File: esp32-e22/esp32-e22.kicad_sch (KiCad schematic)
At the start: 20 parts, among them J1 Conn_01x04_Socket, J2 Conn_01x04_Socket, J3 Conn_01x04_Socket, J4 Conn_01x03_Socket, J5 SMA, J6 Conn_01x02_Pin, J7 USB_C_Receptacle_PowerOnly_6P, J8 Conn_01x04_Socket, J9 Conn_01x02_Pin, SW1 SW_Push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

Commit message: fixed some missing footprints -> V2.0.5
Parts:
- removed J6: Conn_01x02_Pin, Connector_PinHeader_2.54mm:PinHeader_1x02_P2.54mm_Vertical, symbol Connector:Conn_01x02_Pin
- removed J9: Conn_01x02_Pin, symbol Connector:Conn_01x02_Pin
- added J6, J9: Conn_01x02_Socket, Connector_PinHeader_2.54mm:PinHeader_1x02_P2.54mm_Vertical, symbol Connector:Conn_01x02_Socket
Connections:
- net +5V: now also J9.1 (Pin_1)
- net GND: now also J6.2 (Pin_2), J9.2 (Pin_2)
- net at U1.8 (DIO2): now also J6.1 (Pin_1)
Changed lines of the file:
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@@
 		(title "ESP32 - E22 Board")
 		(date "2024-10-04")
-		(rev "V2.0.4")
+		(rev "V2.0.5")
 		(company "DK9BT / OE3WAS")
 	)
@@
 	(wire
 		(pts
-			(xy 82.55 149.86) (xy 82.55 153.67)
-		)
-		(stroke
-			(width 0)
-			(type default)
-		)
-	)
-	(wire
-		(pts
 			(xy 53.34 105.41) (xy 194.31 105.41)
 		)
@@
 	(wire
 		(pts
+			(xy 82.55 149.86) (xy 82.55 153.67)
+		)
+		(stroke
+			(width 0)
+			(type default)
+		)
+	)
+	(wire
+		(pts
 			(xy 181.61 58.42) (xy 217.17 58.42)
 		)
@@
 	)
 	(symbol
-		(lib_id "Connector:Conn_01x02_Pin")
-		(at 77.47 147.32 0)
+		(lib_id "power:+3.3V")
+		(at 160.02 85.09 0)
 		(unit 1)
 		(exclude_from_sim no)
@@
 		(on_board yes)
 		(dnp no)
-		(fields_autoplaced yes)
-		(property "Reference" "J9"
-			(at 76.2 148.5899 0)
+		(property "Reference" "#PWR015"
+			(at 160.02 88.9 0)
 			(effects
 				(font
 					(size 1.27 1.27)
 				)
-				(justify right)
+				(hide yes)
 			)
 		)
-		(property "Value" "Conn_01x02_Pin"
-			(at 78.105 144.78 0)
+		(property "Value" "+3.3V"
+			(at 157.734 81.28 0)
 			(effects
 				(font
 					(size 1.27 1.27)
 				)
-				(hide yes)
+				(justify left)
 			)
 		)
 		(property "Footprint" ""
-			(at 77.47 147.32 0)
+			(at 160.02 85.09 0)
 			(effects
 				(font
@@
 			)
 		)
-		(property "Datasheet" "~"
-			(at 77.47 147.32 0)
+		(property "Datasheet" ""
+			(at 160.02 85.09 0)
 			(effects
 				(font
@@
 			)
 		)
-		(property "Description" "Generic connector, single row, 01x02, script generated"
-			(at 77.47 147.32 0)
+		(property "Description" "Power symbol creates a global label with name \"+3.3V\""
+			(at 160.02 85.09 0)
 			(effects
 				(font
@@
 			)
 		)
-		(pin "2"
-		)
 		(pin "1"
 		)
@@
 			(project "esp32-e22"
 				(path "/7ac59502-473d-4014-a9ef-f4cf3cefb926"
-					(reference "J9")
+					(reference "#PWR015")
 					(unit 1)
 				)
@@
 	)
 	(symbol
-		(lib_id "power:+3.3V")
-		(at 160.02 85.09 0)
+		(lib_id "Device:C_Small")
+		(at 132.08 147.32 0)
 		(unit 1)
 		(exclude_from_sim no)
@@
 		(on_board yes)
 		(dnp no)
-		(property "Reference" "#PWR015"
-			(at 160.02 88.9 0)
+		(property "Reference" "C4"
+			(at 134.366 145.542 0)
 			(effects
 				(font
 					(size 1.27 1.27)
 				)
-				(hide yes)
+				(justify left)
 			)
 		)
-		(property "Value" "+3.3V"
-			(at 157.734 81.28 0)
+		(property "Value" "100nF"
+			(at 134.366 147.828 0)
 			(effects
 				(font
@@
 			)
 		)
-		(property "Footprint" ""
-			(at 160.02 85.09 0)
+		(property "Footprint" "Capacitor_THT:C_Disc_D4.7mm_W2.5mm_P5.00mm"
+			(at 132.08 147.32 0)
 			(effects
 				(font
@@
 			)
 		)
-		(property "Datasheet" ""
-			(at 160.02 85.09 0)
+		(property "Datasheet" "~"
+			(at 132.08 147.32 0)
 			(effects
 				(font
@@
 			)
 		)
-		(property "Description" "Power symbol creates a global label with name \"+3.3V\""
-			(at 160.02 85.09 0)
+		(property "Description" "Unpolarized capacitor, small symbol"
+			(at 132.08 147.32 0)
 			(effects
 				(font
@@
 		(pin "1"
 		)
+		(pin "2"
+		)
 		(instances
 			(project "esp32-e22"
 				(path "/7ac59502-473d-4014-a9ef-f4cf3cefb926"
-					(reference "#PWR015")
+					(reference "C4")
 					(unit 1)
 				)
@@
 	)
 	(symbol
-		(lib_id "Device:C_Small")
-		(at 132.08 147.32 0)
+		(lib_id "Connector:Conn_01x02_Socket")
+		(at 77.47 147.32 0)
+		(mirror y)
 		(unit 1)
 		(exclude_from_sim no)
@@
 		(on_board yes)
 		(dnp no)
-		(property "Reference" "C4"
-			(at 134.366 145.542 0)
+		(property "Reference" "J9"
+			(at 78.105 154.94 0)
 			(effects
 				(font
 					(size 1.27 1.27)
 				)
-				(justify left)
 			)
 		)
-		(property "Value" "100nF"
-			(at 134.366 147.828 0)
+		(property "Value" "Conn_01x02_Socket"
+			(at 66.294 148.082 0)
 			(effects
 				(font
 					(size 1.27 1.27)
 				)
-				(justify left)
 			)
 		)
-		(property "Footprint" "Capacitor_THT:C_Disc_D4.7mm_W2.5mm_P5.00mm"
-			(at 132.08 147.32 0)
+		(property "Footprint" "Connector_PinHeader_2.54mm:PinHeader_1x02_P2.54mm_Vertical"
+			(at 77.47 147.32 0)
 			(effects
 				(font
@@
 		)
 		(property "Datasheet" "~"
-			(at 132.08 147.32 0)
+			(at 77.47 147.32 0)
 			(effects
 				(font
@@
 			)
 		)
-		(property "Description" "Unpolarized capacitor, small symbol"
-			(at 132.08 147.32 0)
+		(property "Description" "Generic connector, single row, 01x02, script generated"
+			(at 77.47 147.32 0)
 			(effects
 				(font
@@
 			(project "esp32-e22"
 				(path "/7ac59502-473d-4014-a9ef-f4cf3cefb926"
-					(reference "C4")
+					(reference "J9")
 					(unit 1)
 				)
@@
 	)
 	(symbol
-		(lib_id "Connector:Conn_01x02_Pin")
-		(at 260.35 55.88 0)
-		(mirror y)
-		(unit 1)
-		(exclude_from_sim no)
-		(in_bom yes)
-		(on_board yes)
-		(dnp no)
-		(fields_autoplaced yes)
-		(property "Reference" "J6"
-			(at 261.62 57.1499 0)
-			(effects
-				(font
-					(size 1.27 1.27)
-				)
-				(justify right)
-			)
-		)
-		(property "Value" "Conn_01x02_Pin"
-			(at 259.715 53.34 0)
-			(effects
-				(font
-					(size 1.27 1.27)
-				)
-				(hide yes)
-			)
-		)
-		(property "Footprint" "Connector_PinHeader_2.54mm:PinHeader_1x02_P2.54mm_Vertical"
-			(at 260.35 55.88 0)
-			(effects
-				(font
-					(size 1.27 1.27)
-				)
-				(hide yes)
-			)
-		)
-		(property "Datasheet" "~"
-			(at 260.35 55.88 0)
-			(effects
-				(font
-					(size 1.27 1.27)
-				)
-				(hide yes)
-			)
-		)
-		(property "Description" "Generic connector, single row, 01x02, script generated"
-			(at 260.35 55.88 0)
-			(effects
-				(font
-					(size 1.27 1.27)
-				)
-				(hide yes)
-			)
-		)
-		(pin "2"
-		)
-		(pin "1"
-		)
-		(instances
-			(project ""
-				(path "/7ac59502-473d-4014-a9ef-f4cf3cefb926"
-					(reference "J6")
-					(unit 1)
-				)
-			)
-		)
-	)
-	(symbol
 		(lib_id "E22:E22_400M33S")
 		(at 219.71 44.45 0)
@@
 					(unit 1)
 				)
+			)
+		)
+	)
+	(symbol
+		(lib_id "Connector:Conn_01x02_Socket")
+		(at 260.35 55.88 0)
+		(unit 1)
+		(exclude_from_sim no)
+		(in_bom yes)
+		(on_board yes)
+		(dnp no)
+		(fields_autoplaced yes)
+		(property "Reference" "J6"
+			(at 261.62 55.8799 0)
+			(effects
+				(font
+					(size 1.27 1.27)
+				)
+				(justify left)
+			)
+		)
+		(property "Value" "Conn_01x02_Socket"
+			(at 261.62 58.4199 0)
+			(effects
+				(font
+					(size 1.27 1.27)
+				)
+				(justify left)
+			)
+		)
+		(property "Footprint" "Connector_PinHeader_2.54mm:PinHeader_1x02_P2.54mm_Vertical"
+			(at 260.35 55.88 0)
+			(effects
+				(font
+					(size 1.27 1.27)
+				)
+				(hide yes)
+			)
+		)
+		(property "Datasheet" "~"
+			(at 260.35 55.88 0)
+			(effects
+				(font
+					(size 1.27 1.27)
+				)
+				(hide yes)
+			)
+		)
+		(property "Description" "Generic connector, single row, 01x02, script generated"
+			(at 260.35 55.88 0)
+			(effects
+				(font
+					(size 1.27 1.27)
+				)
+				(hide yes)
+			)
+		)
+		(pin "1"
+		)
+		(pin "2"
+		)
+		(instances
+			(project ""
+				(path "/7ac59502-473d-4014-a9ef-f4cf3cefb926"
+					(reference "J6")
+					(unit 1)
+				)

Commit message: update to v2.0.6
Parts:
- added C5: 100nF, Capacitor_THT:C_Disc_D4.7mm_W2.5mm_P5.00mm, symbol Device:C_Small
- added C6: 10µF, Capacitor_THT:CP_Radial_D6.3mm_P2.50mm, symbol Device:C_Polarized
- added J10: Conn_01x02_Socket, Connector_PinHeader_2.54mm:PinHeader_1x02_P2.54mm_Vertical, symbol Connector:Conn_01x02_Socket
- added R3, R4: 5.1k, Resistor_THT:R_Axial_DIN0207_L6.3mm_D2.5mm_P7.62mm_Horizontal, symbol Device:R
- J9: footprint Connector_PinHeader_2.54mm:PinHeader_1x02_P2.54mm_Vertical -> TerminalBlock_Phoenix:TerminalBlock_Phoenix_MKDS-1,5-2-5.08_1x02_P5.08mm_Horizontal
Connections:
- net +3.3V: now also C4.1
- net +5V: now also C1.1; no longer C1.2, C4.1
- net GND: now also C1.2, C5.2, C6.2, J10.2 (Pin_2), R4.2; no longer C1.1
- net at U2.2 (CHIP_PU): now also C6.1
- net at U2.7 (32K_XP/GPIO32/ADC1_CH4): now also C5.1, R3.2, R4.1
- new net: J10.1 (Pin_1), R3.1
- no-connect marks 19 -> 17
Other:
- moved on the sheet: C1, C2, C3, C4, J1, J2, J3, J4, J5, J6, J7, J8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

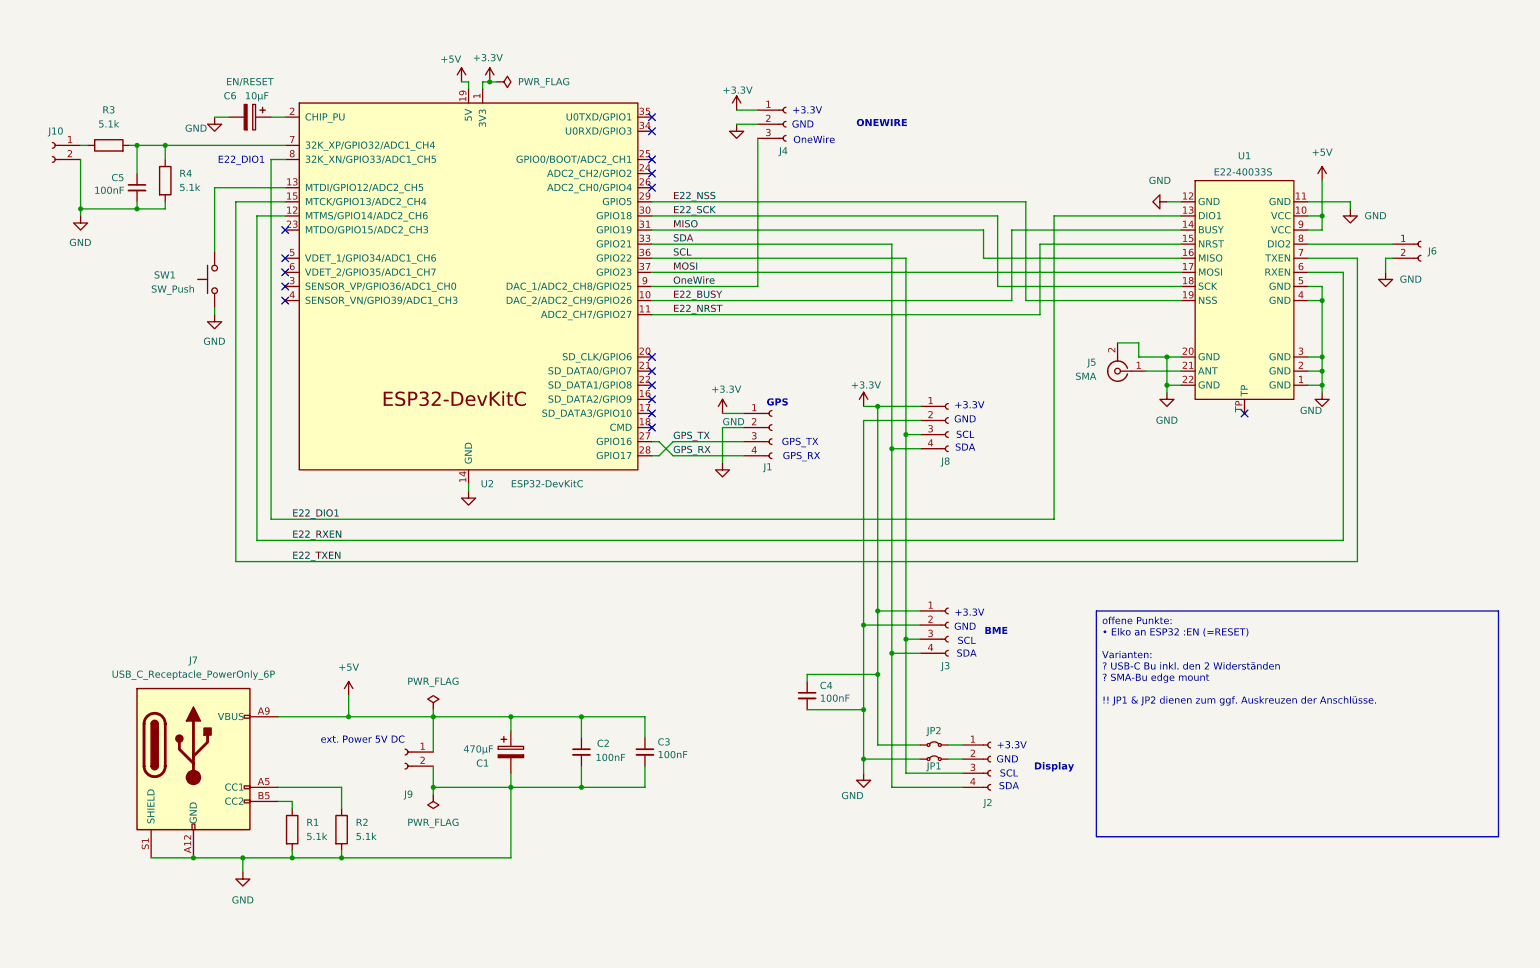
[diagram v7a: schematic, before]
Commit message: update to v2.0.7
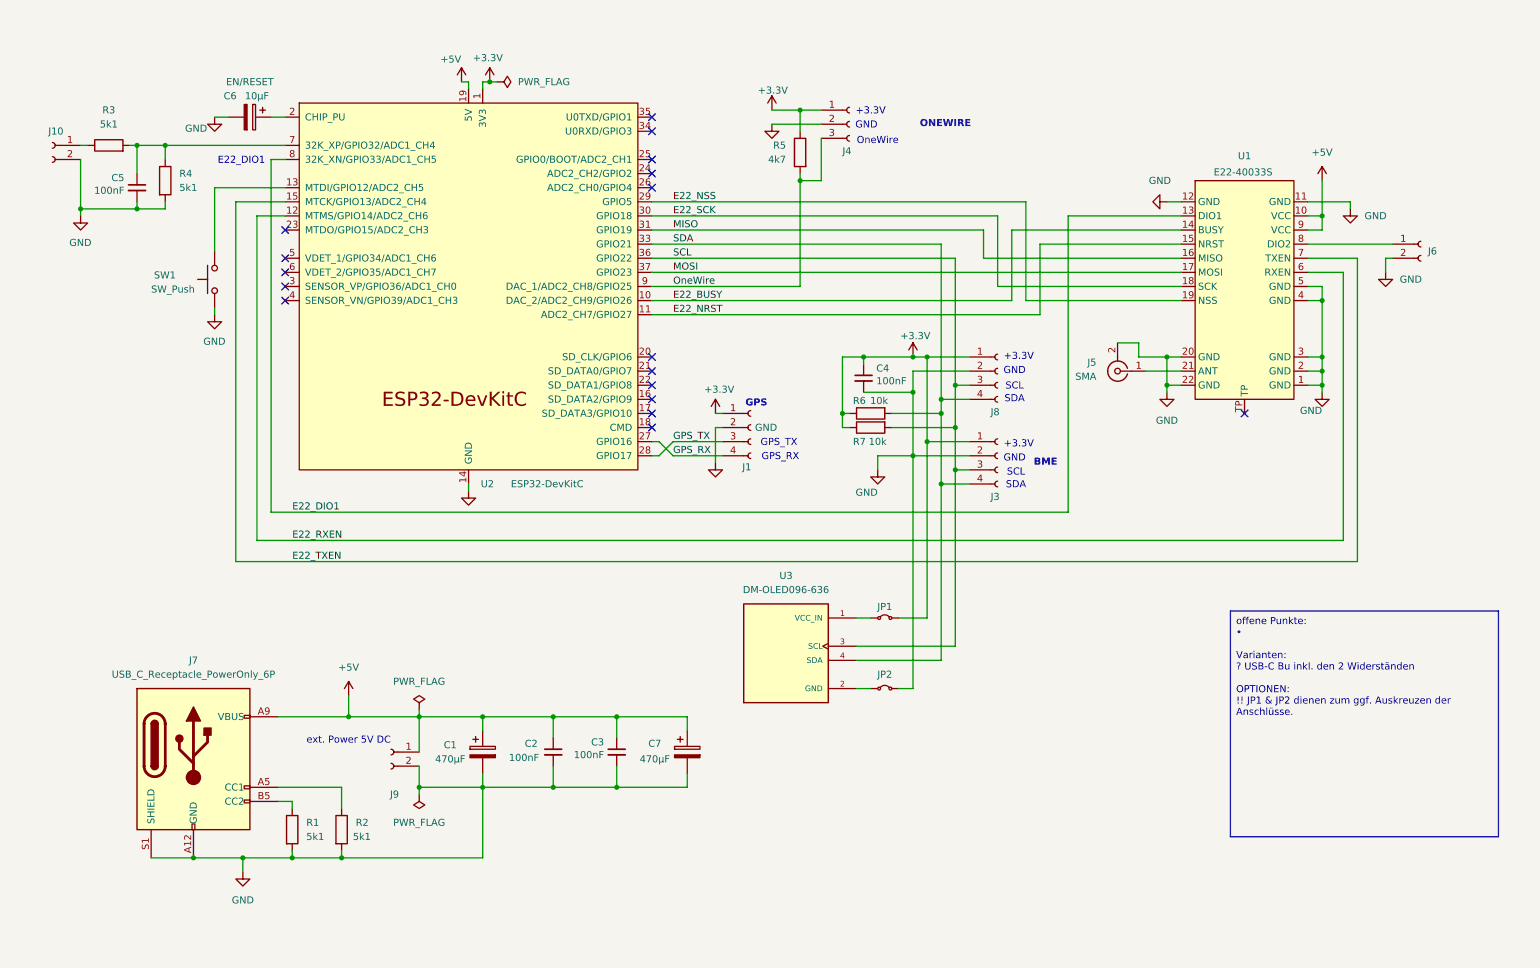
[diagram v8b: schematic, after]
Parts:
- removed J2: Conn_01x04_Socket, Connector_PinHeader_2.54mm:PinHeader_1x04_P2.54mm_Vertical, symbol Connector:Conn_01x04_Socket
- added C7: 470µF, Capacitor_THT:CP_Radial_D8.0mm_P5.00mm, symbol Device:C_Polarized
- added R5: 4k7, Resistor_THT:R_Axial_DIN0207_L6.3mm_D2.5mm_P7.62mm_Horizontal, symbol Device:R
- added R6, R7: 10k, Resistor_THT:R_Axial_DIN0207_L6.3mm_D2.5mm_P7.62mm_Horizontal, symbol Device:R
- added U3: DM-OLED096-636, E22:DM-OLED096-636, symbol DM-OLED096-636:DM-OLED096-636
- R1, R2, R3, R4: value 5.1k -> 5k1
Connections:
- net +3.3V: now also JP1.2 (B), R5.1, R6.1, R7.1; no longer JP2.1 (A)
- net +5V: now also C7.1
- net GND: now also JP2.2 (B), C7.2; no longer JP1.1 (A)
- net OneWire: now also R5.2
- net SCL: now also R7.2, U3.3 (SCL)
- net SDA: now also R6.2, U3.4 (SDA)
- new net: JP1.1 (A), U3.1 (VCC_IN)
- new net: JP2.1 (A), U3.2 (GND)
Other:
- note removed: "Display"
- moved on the sheet: C1, C2, C3, C4, J1, J3, J4, J8, J9, JP1, JP2
